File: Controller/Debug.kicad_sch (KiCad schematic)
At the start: 18 parts

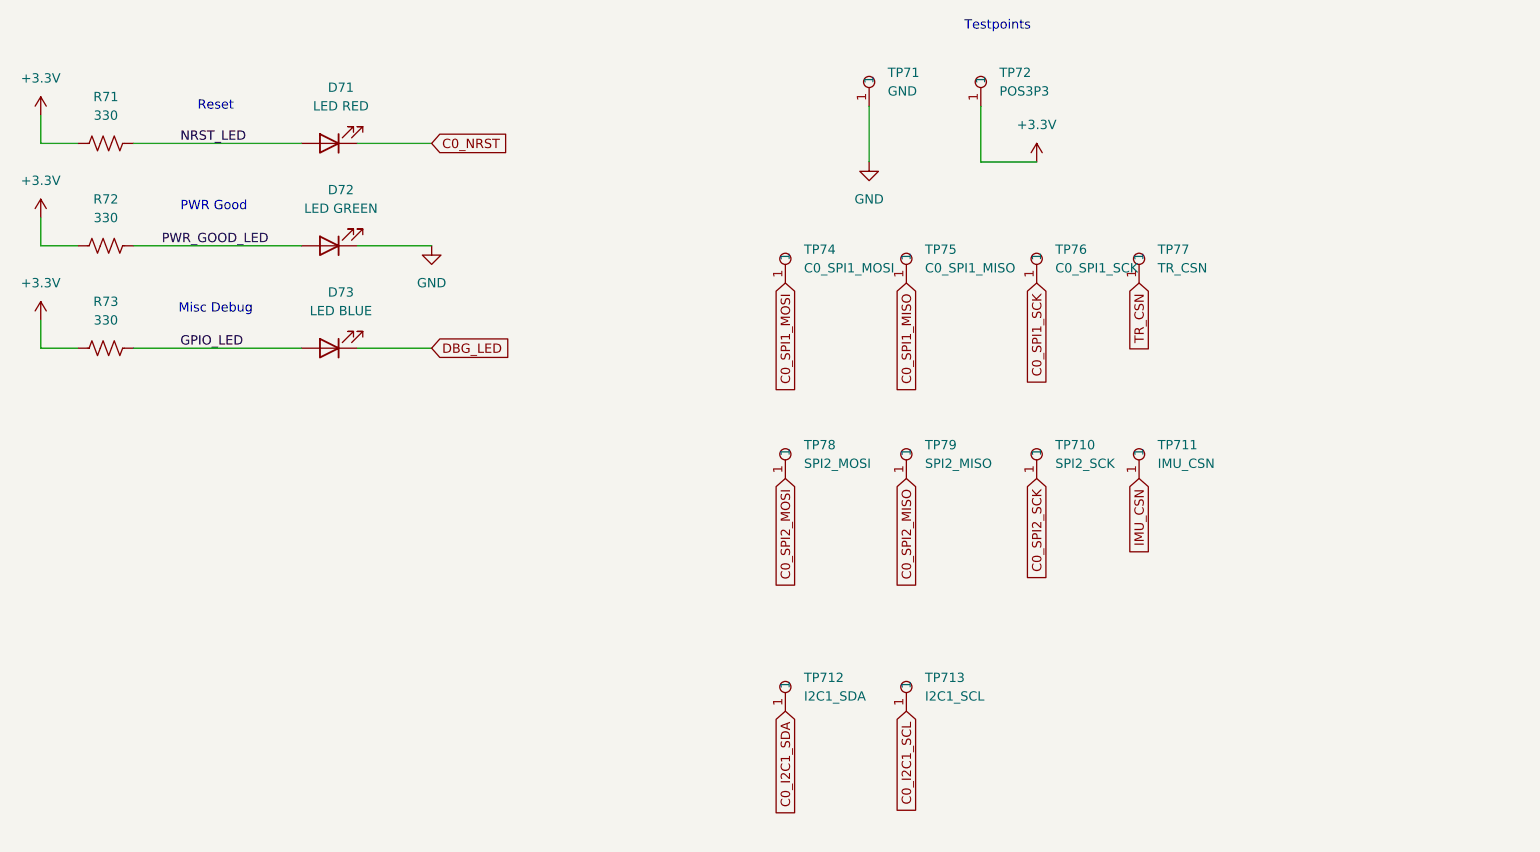
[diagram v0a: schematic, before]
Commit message: Finished Schematic for controller
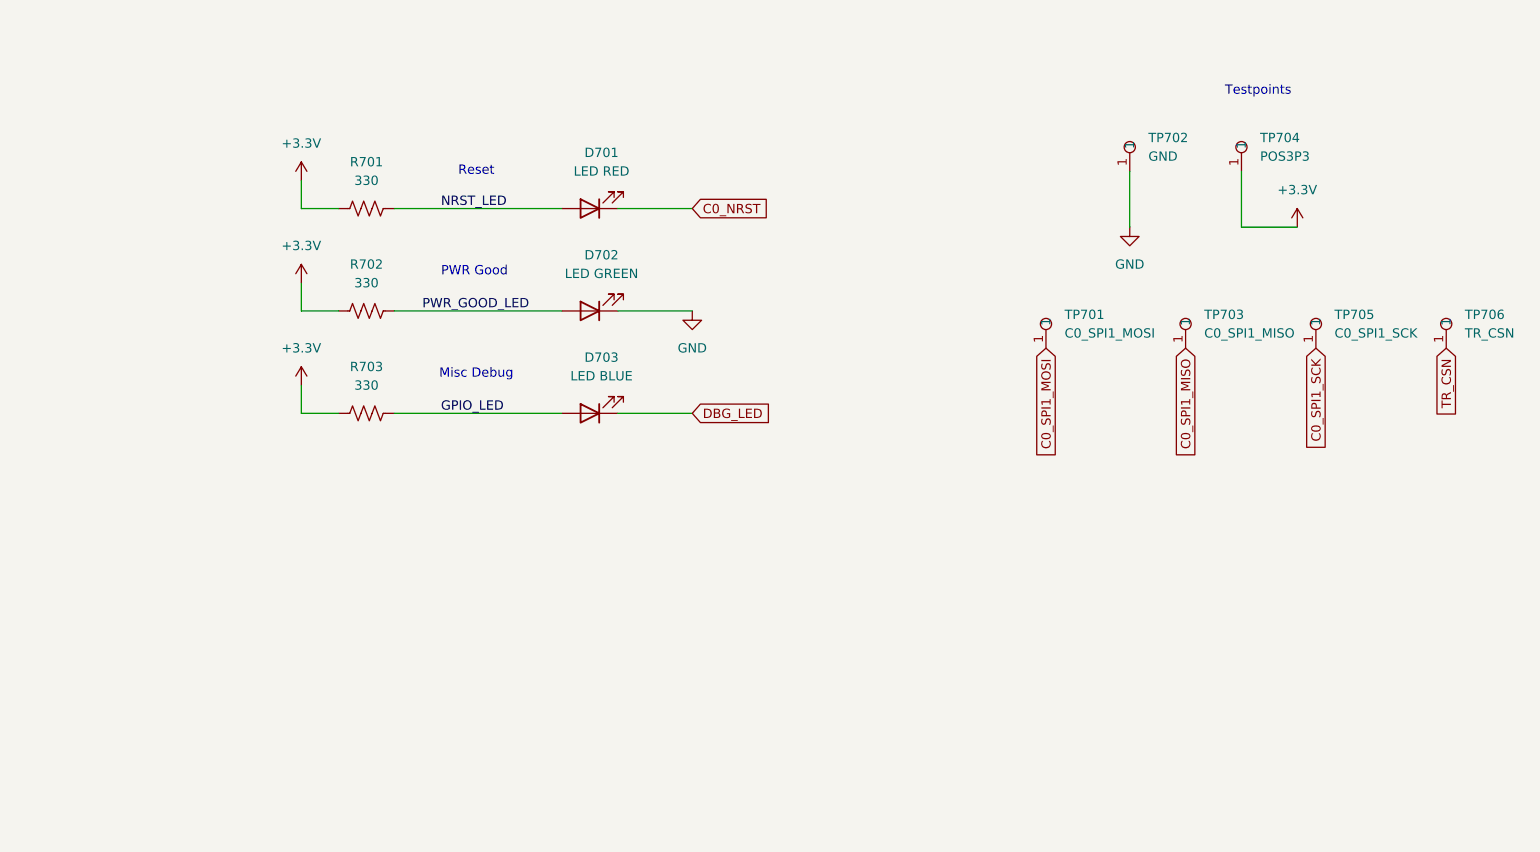
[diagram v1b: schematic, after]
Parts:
- removed TP710: SPI2_SCK, Library:Testpoint 1.6mm x 0.8mm, symbol Global:Testpoint
- removed TP711: IMU_CSN, Library:Testpoint 1.6mm x 0.8mm, symbol Global:Testpoint
- removed TP712: I2C1_SDA, Library:Testpoint 1.6mm x 0.8mm, symbol Global:Testpoint
- removed TP713: I2C1_SCL, Library:Testpoint 1.6mm x 0.8mm, symbol Global:Testpoint
- removed TP78: SPI2_MOSI, Library:Testpoint 1.6mm x 0.8mm, symbol Global:Testpoint
- removed TP79: SPI2_MISO, Library:Testpoint 1.6mm x 0.8mm, symbol Global:Testpoint
- renumbered D71 to D701, D72 to D702, D73 to D703, R71 to R701, R72 to R702, R73 to R703, TP74 to TP701, TP71 to TP702, TP75 to TP703, TP72 to TP704, TP76 to TP705, TP77 to TP706
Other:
- moved on the sheet: D701, D702, D703, R701, R702, R703, TP701, TP702, TP703, TP704, TP705, TP706
